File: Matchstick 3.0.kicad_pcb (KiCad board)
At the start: 2 copper layers, 47.2 x 34 mm, 9 parts, among them J3 Barrel_Jack, J4 Screw_Terminal_01x08, SW1 SparkFun_COM-08720, U1 M5StampS3

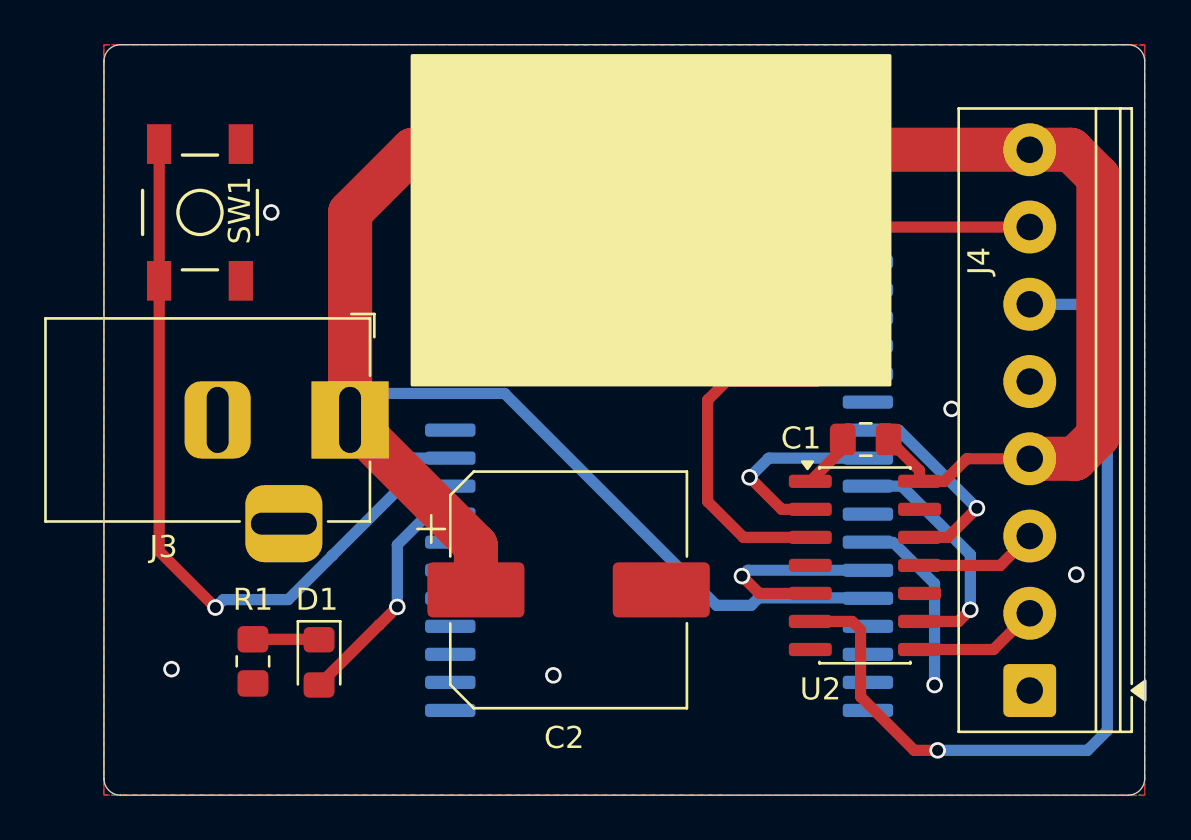
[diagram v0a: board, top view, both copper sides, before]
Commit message: silkscreen & logo update
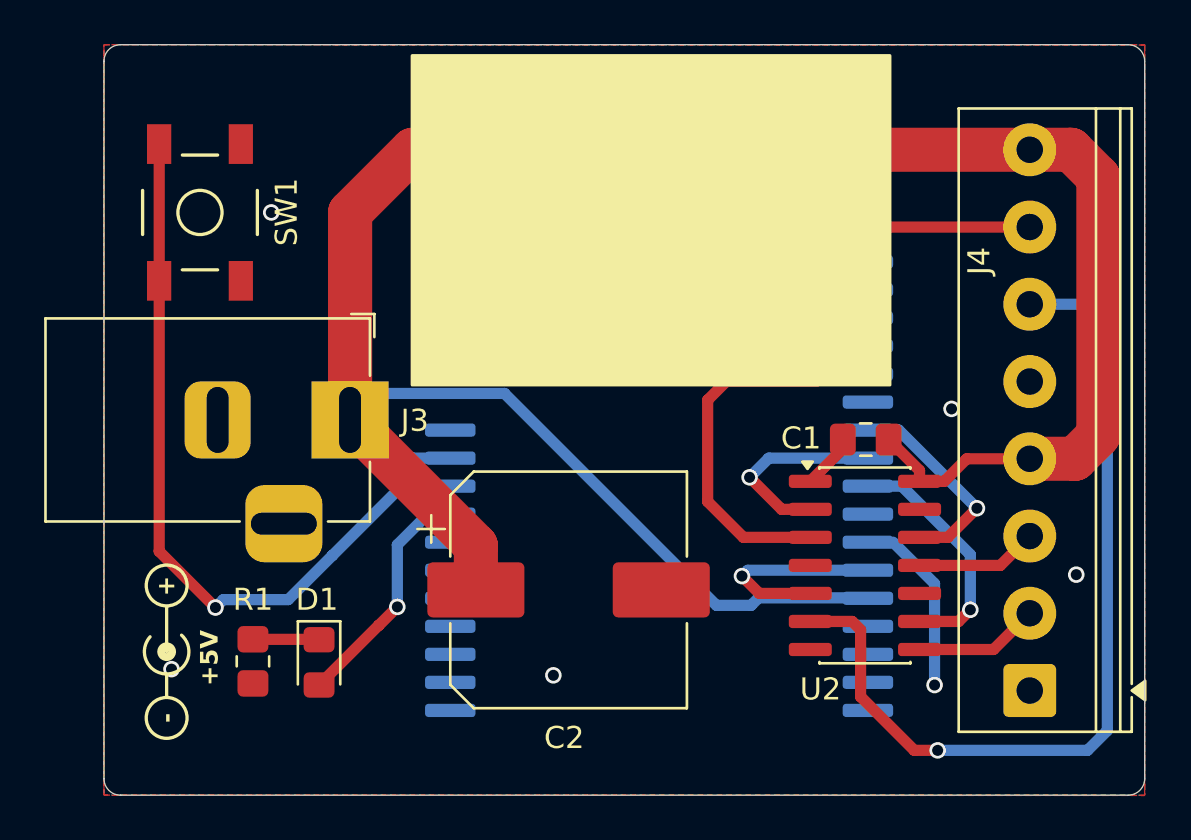
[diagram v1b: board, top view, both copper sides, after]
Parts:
- added REF**: Symbol_Barrel_Polarity, Symbol:Symbol_Barrel_Polarity, F.Cu at (161.6, 115.0)
- added REF**: Cat1-Logo_15x8.7mm_SilkScreen, Logo:Cat1-Logo_15x8.7mm_SilkScreen, B.Cu at (166.5, 116.8)
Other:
- board text added: "+"
- board text added: "+5V"
- board text added: "-"

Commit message: added prod no. location for PCBWay
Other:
- board text added: "WayWayWay"
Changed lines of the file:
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@@
+		)
+	)
+	(gr_text "WayWayWay"
+		(at 192 118.95 0)
+		(layer "B.SilkS")
+		(effects
+			(font
+				(size 0.8 0.8)
+				(thickness 0.15)
+				(bold yes)
+			)
+			(justify left bottom mirror)
 		)
 	)
